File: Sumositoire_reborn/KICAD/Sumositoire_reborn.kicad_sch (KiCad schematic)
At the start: 47 parts, among them J1 Conn_01x04, J11 batt, J12 inter, J13 CNY_AV, J2 CNY_AR, J3 MOTEUR1, J4 MOTEUR2, J5 CAPT_ULTRASON, J6 CAPT_INFRA_1, J7 CAPT_INFRA_2, J8 CAPT_INFRA_3, SW1 SW_Push, U1 ATmega328P-AU_full, U3 LD1117S50TR_SOT223, U4 DRV8835, U5 TSOP18338, Y1 Crystal_GND2

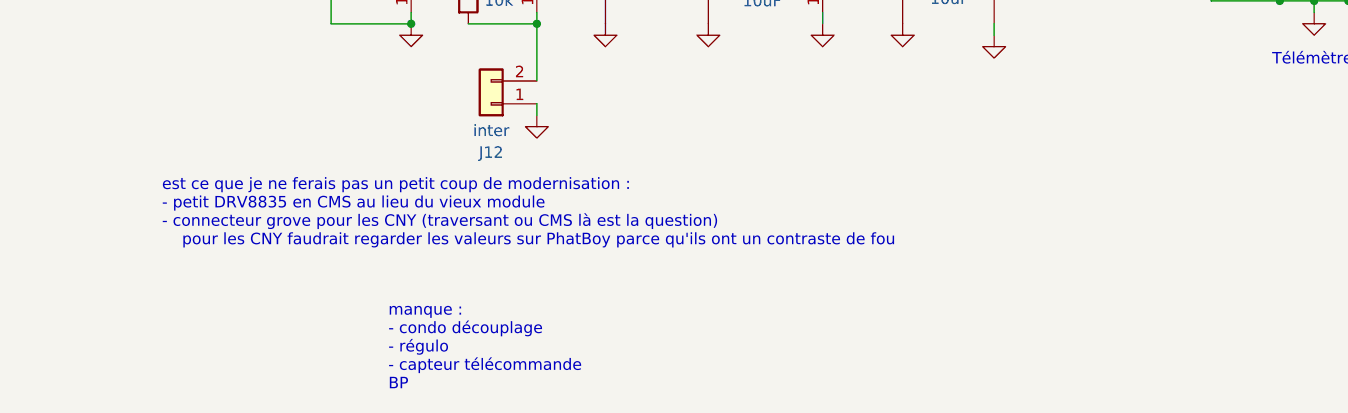
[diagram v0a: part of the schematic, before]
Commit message: suppression de commentaires sur les pistes d'amélioration du robot qui ont été corrigées
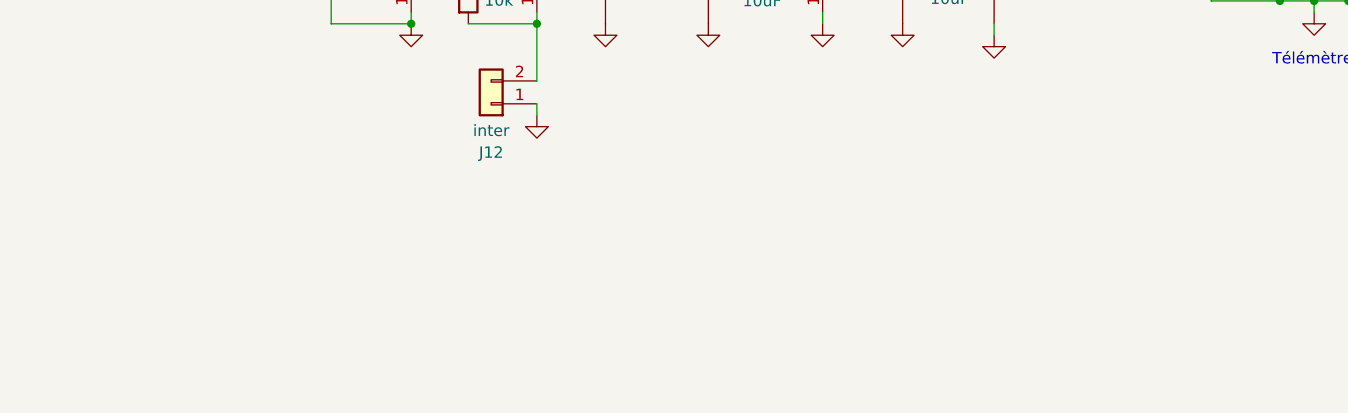
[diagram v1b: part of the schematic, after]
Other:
- note removed: "est ce que je ne ferais pas un petit coup de modernisation : - petit DRV8835 en CMS au lieu du vieux module - connecteur grove pour les CNY (traversant ou CMS là est la question) pour les CNY faudrait regarder les valeurs sur PhatBoy parce qu'ils ont un contraste de fou"
- note removed: "manque : - condo découplage - régulo - capteur télécommande BP"
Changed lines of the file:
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@@
-		)
-	)
-	(text "est ce que je ne ferais pas un petit coup de modernisation :\n- petit DRV8835 en CMS au lieu du vieux module\n- connecteur grove pour les CNY (traversant ou CMS là est la question)\n	pour les CNY faudrait regarder les valeurs sur PhatBoy parce qu'ils ont un contraste de fou"
-		(exclude_from_sim no)
-		(at 92.964 169.672 0)
-		(effects
-			(font
-				(size 1.27 1.27)
-			)
-			(justify left)
 		)
 	)
@@
 		)
 	)
-	(text "manque :\n- condo découplage\n- régulo\n- capteur télécommande\nBP\n"
-		(exclude_from_sim no)
-		(at 118.11 184.658 0)
-		(effects
-			(font
-				(size 1.27 1.27)
-			)
-			(justify left)
-		)
-	)
